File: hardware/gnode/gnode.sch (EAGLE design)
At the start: 8 parts, among them U1 ATMEGA328P_TQFP, U2 3.3V/150mA

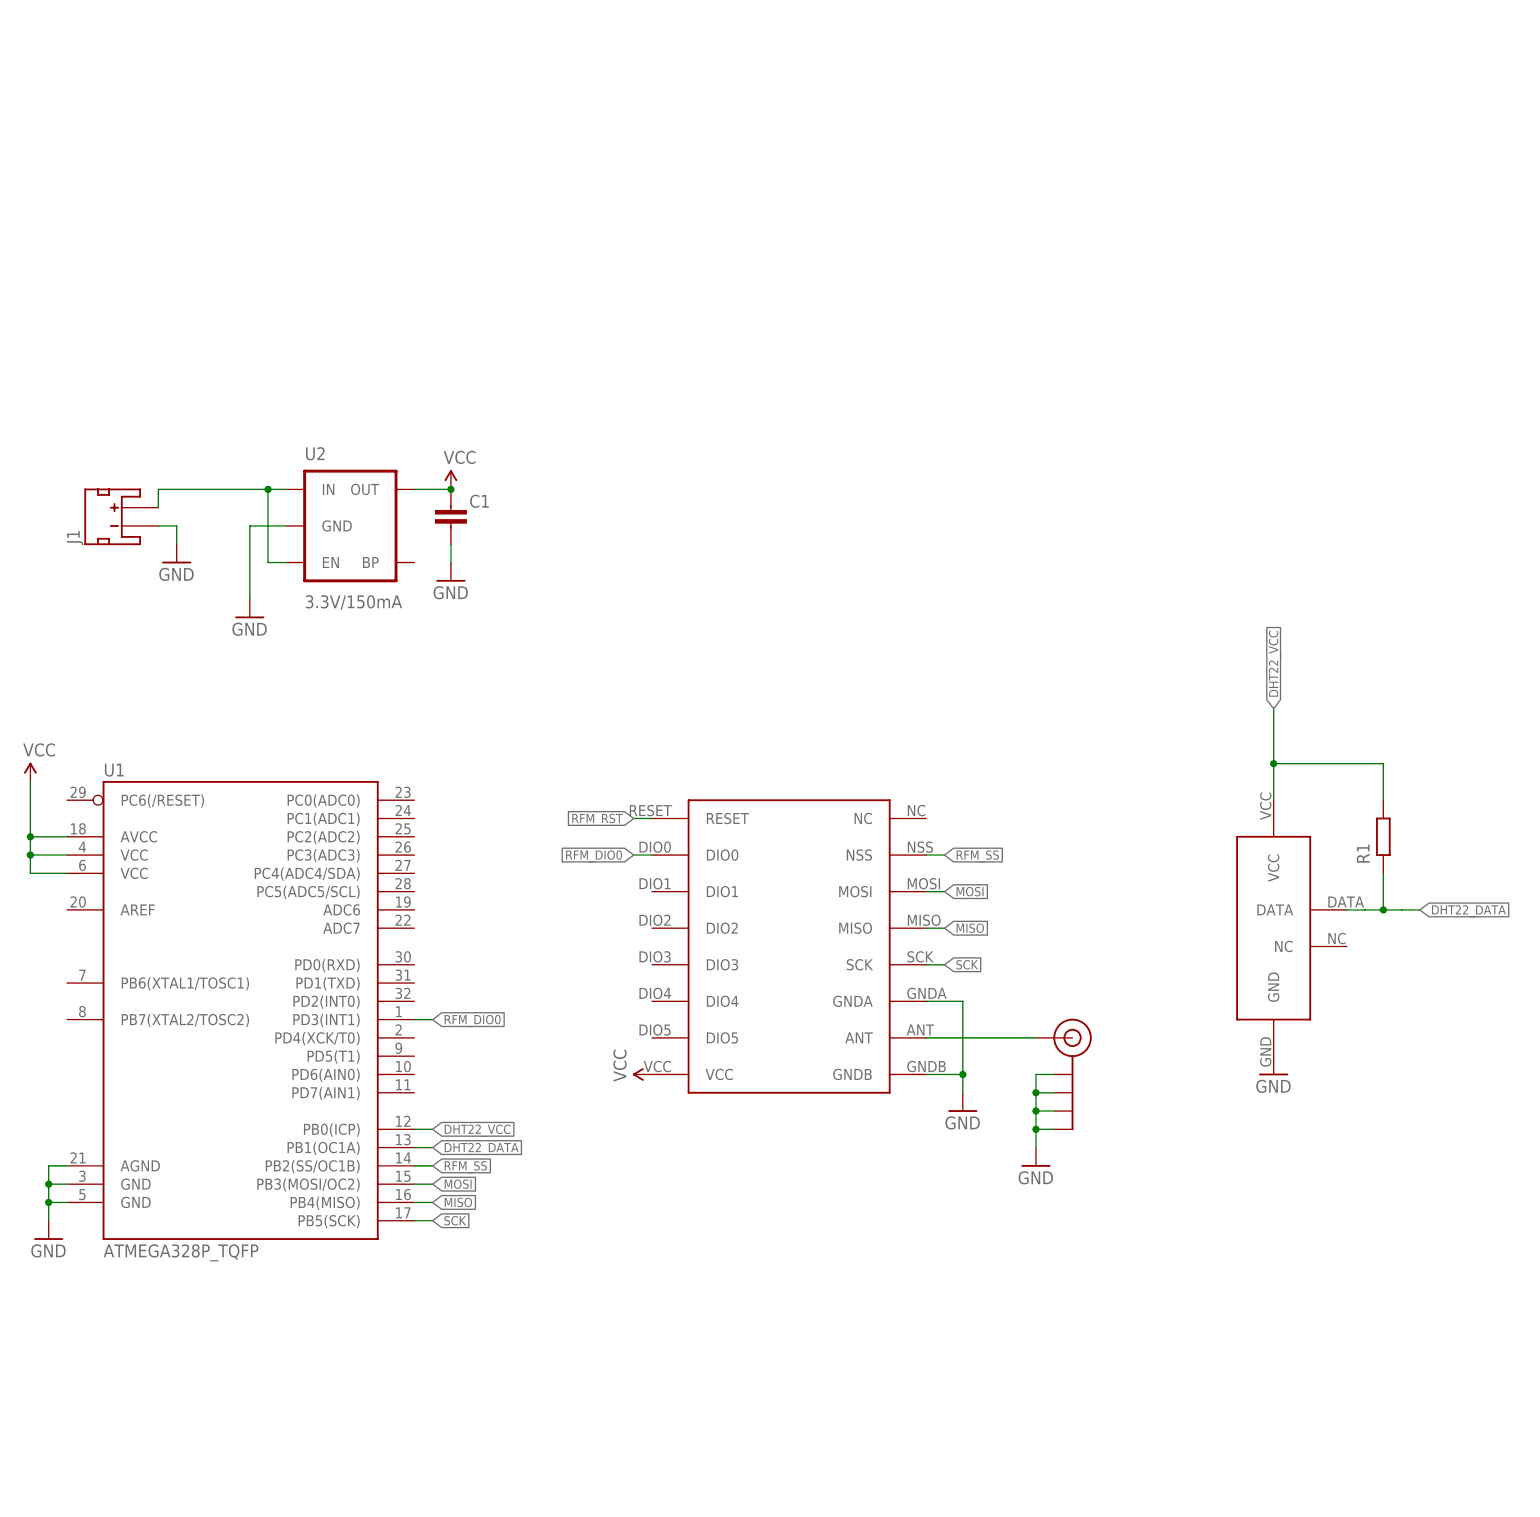
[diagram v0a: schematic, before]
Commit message: reduced to r25mm, added htu21d and icsp header
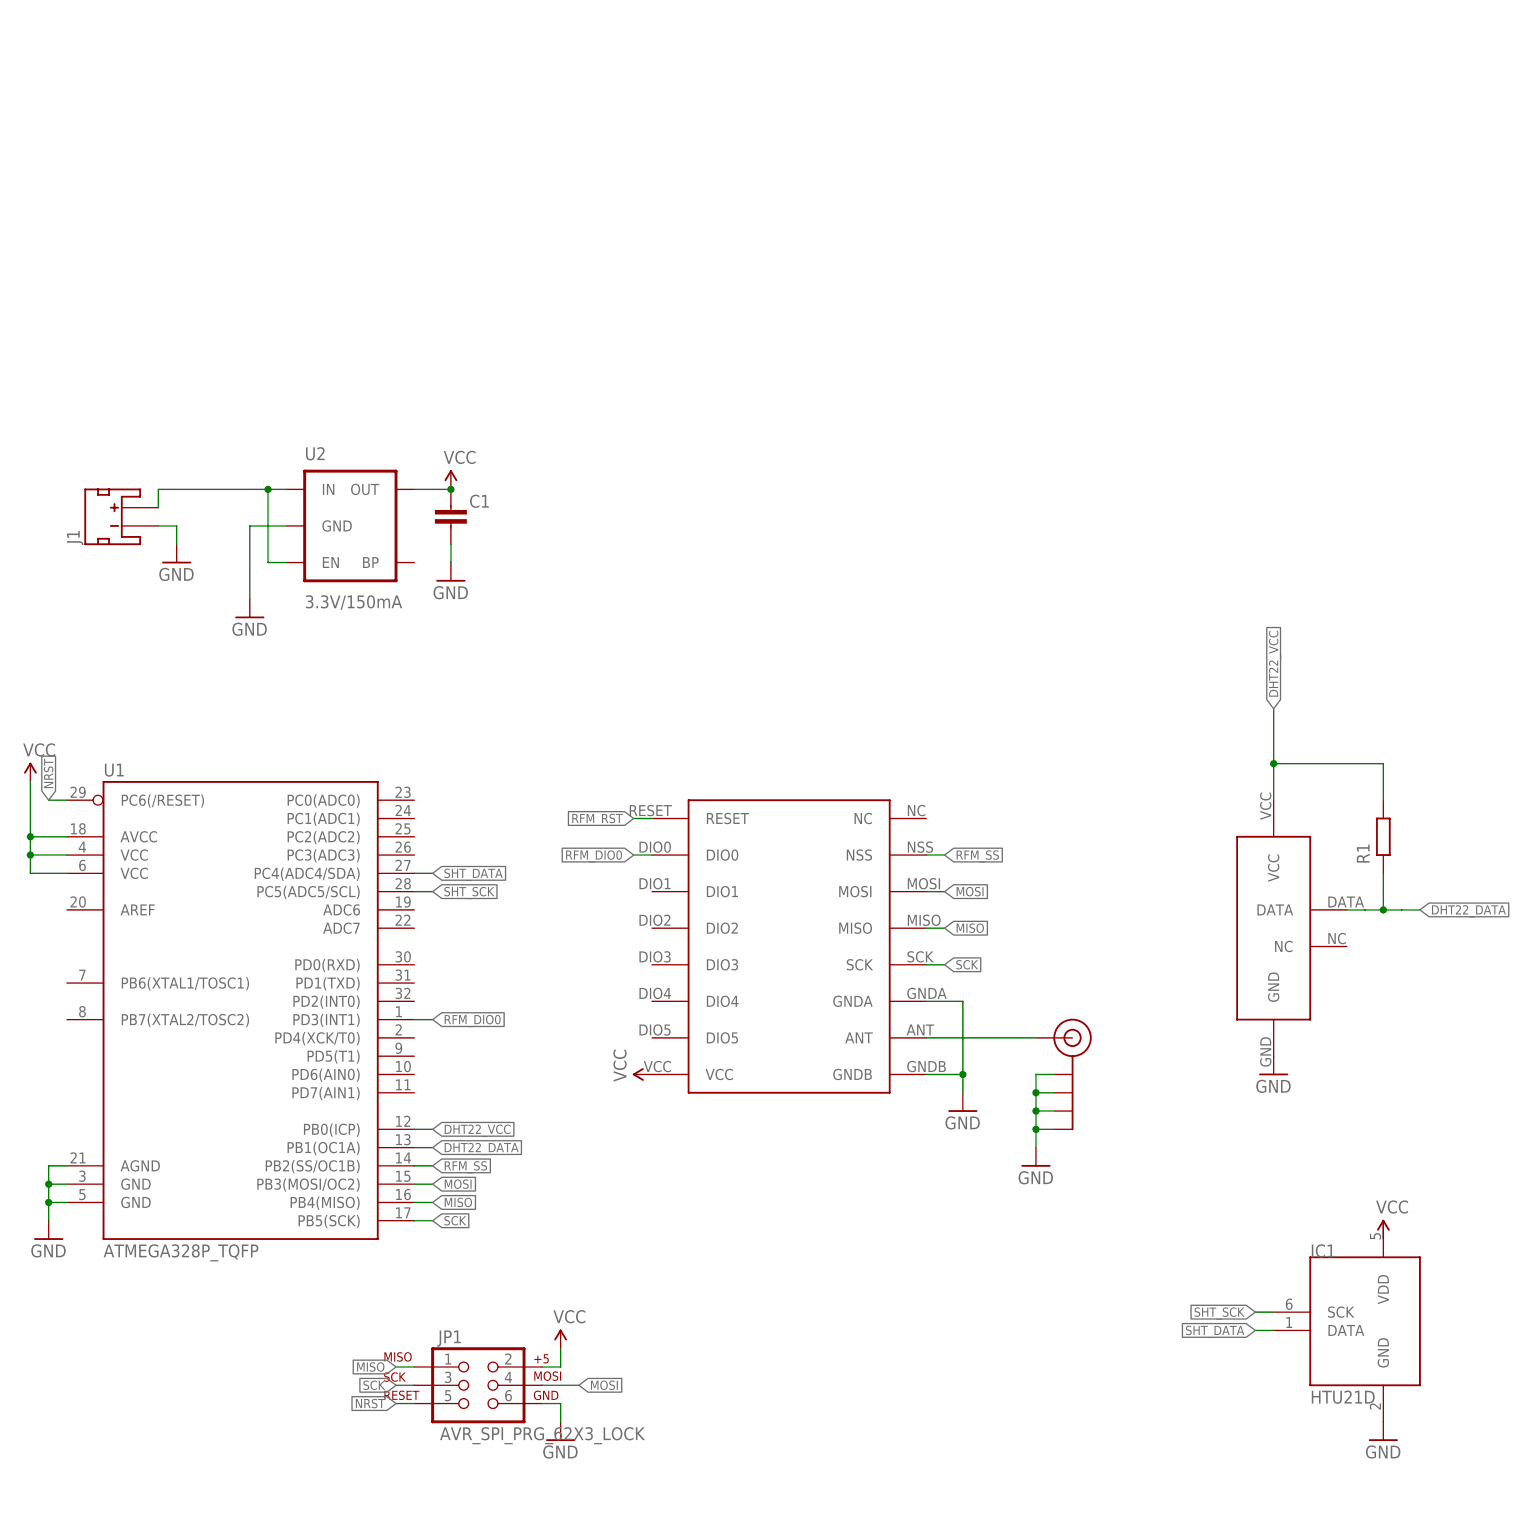
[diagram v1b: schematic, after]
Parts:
- added IC1: HTU21D, Mine:HTU21D
- added JP1: AVR_SPI_PRG_62X3_LOCK, SparkFun-Connectors:AVR_SPI_PRG_62X3_LOCK
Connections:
- new net NRST: JP1.5, U1.PC6(/RESET)
- new net SHT_DATA: IC1.DATA, U1.PC4(ADC4/SDA)
- new net SHT_SCK: IC1.SCK, U1.PC5(ADC5/SCL)
- net GND: now also IC1.GND, JP1.6
- net MISO: now also JP1.1
- net MOSI: now also JP1.4
- net SCK: now also JP1.3
- net VCC: now also JP1.2
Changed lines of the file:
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@@
 <setting verticaltext="up"/>
 </settings>
-<grid distance="0.1" unitdist="inch" unit="inch" style="lines" multiple="1" display="yes" altdistance="0.005" altunitdist="inch" altunit="inch"/>
+<grid distance="0.1" unitdist="inch" unit="inch" style="lines" multiple="1" display="no" altdistance="0.01" altunitdist="inch" altunit="inch"/>
 <layers>
 <layer number="1" name="Top" color="4" fill="1" visible="no" active="no"/>
@@
 <part name="SUPPLY3" library="SparkFun-Aesthetics" deviceset="VCC" device=""/>
 <part name="GND7" library="SparkFun-Aesthetics" deviceset="GND" device=""/>
+<part name="IC1" library="Mine" deviceset="HTU21D" device=""/>
+<part name="SUPPLY4" library="SparkFun-Aesthetics" deviceset="VCC" device=""/>
+<part name="GND8" library="SparkFun-Aesthetics" deviceset="GND" device=""/>
+<part name="JP1" library="SparkFun-Connectors" deviceset="AVR_SPI_PRG_6" device="2X3_LOCK"/>
+<part name="SUPPLY5" library="SparkFun-Aesthetics" deviceset="VCC" device=""/>
+<part name="GND9" library="SparkFun-Aesthetics" deviceset="GND" device=""/>
 </parts>
 <sheets>
@@
 <instance part="SUPPLY3" gate="G$1" x="17.78" y="109.22"/>
 <instance part="GND7" gate="1" x="17.78" y="96.52"/>
+<instance part="IC1" gate="G$1" x="142.24" y="-7.62"/>
+<instance part="SUPPLY4" gate="G$1" x="147.32" y="5.08"/>
+<instance part="GND8" gate="1" x="147.32" y="-22.86"/>
+<instance part="JP1" gate="G$1" x="20.32" y="-15.24"/>
+<instance part="SUPPLY5" gate="G$1" x="33.02" y="-10.16"/>
+<instance part="GND9" gate="1" x="33.02" y="-22.86"/>
 </instances>
 <busses>
@@
 <wire x1="17.78" y1="99.06" x2="17.78" y2="101.6" width="0.1524" layer="91"/>
 </segment>
+<segment>
+<pinref part="IC1" gate="G$1" pin="GND"/>
+<pinref part="GND8" gate="1" pin="GND"/>
+</segment>
+<segment>
+<pinref part="JP1" gate="G$1" pin="6"/>
+<pinref part="GND9" gate="1" pin="GND"/>
+<wire x1="30.48" y1="-17.78" x2="33.02" y2="-17.78" width="0.1524" layer="91"/>
+<wire x1="33.02" y1="-17.78" x2="33.02" y2="-20.32" width="0.1524" layer="91"/>
+</segment>
 </net>
 <net name="N$1" class="0">
@@
 <label x="15.24" y="12.7" size="1.27" layer="95" font="vector" xref="yes"/>
 </segment>
+<segment>
+<pinref part="JP1" gate="G$1" pin="4"/>
+<wire x1="30.48" y1="-15.24" x2="35.56" y2="-15.24" width="0.1524" layer="91"/>
+<label x="35.56" y="-15.24" size="1.27" layer="95" xref="yes"/>
+</segment>
 </net>
 <net name="MISO" class="0">
@@
 <label x="15.24" y="10.16" size="1.27" layer="95" font="vector" xref="yes"/>
 </segment>
+<segment>
+<pinref part="JP1" gate="G$1" pin="1"/>
+<wire x1="12.7" y1="-12.7" x2="10.16" y2="-12.7" width="0.1524" layer="91"/>
+<label x="10.16" y="-12.7" size="1.27" layer="95" rot="R180" xref="yes"/>
+</segment>
 </net>
 <net name="SCK" class="0">
@@
 <wire x1="12.7" y1="7.62" x2="15.24" y2="7.62" width="0.1524" layer="91"/>
 <label x="15.24" y="7.62" size="1.27" layer="95" font="vector" xref="yes"/>
+</segment>
+<segment>
+<pinref part="JP1" gate="G$1" pin="3"/>
+<wire x1="12.7" y1="-15.24" x2="10.16" y2="-15.24" width="0.1524" layer="91"/>
+<label x="10.16" y="-15.24" size="1.27" layer="95" rot="R180" xref="yes"/>
 </segment>
 </net>
@@
 <junction x="17.78" y="109.22"/>
 </segment>
+<segment>
+<pinref part="JP1" gate="G$1" pin="2"/>
+<pinref part="SUPPLY5" gate="G$1" pin="VCC"/>
+<wire x1="30.48" y1="-12.7" x2="33.02" y2="-12.7" width="0.1524" layer="91"/>
+<wire x1="33.02" y1="-12.7" x2="33.02" y2="-10.16" width="0.1524" layer="91"/>
+</segment>
 </net>
 <net name="N$2" class="0">
@@
 </segment>
 </net>
+<net name="SHT_SCK" class="0">
+<segment>
+<pinref part="IC1" gate="G$1" pin="SCK"/>
+<wire x1="132.08" y1="-5.08" x2="129.54" y2="-5.08" width="0.1524" layer="91"/>
+<label x="129.54" y="-5.08" size="1.27" layer="95" rot="R180" xref="yes"/>
+</segment>
+<segment>
+<pinref part="U1" gate="U$1" pin="PC5(ADC5/SCL)"/>
+<wire x1="12.7" y1="53.34" x2="15.24" y2="53.34" width="0.1524" layer="91"/>
+<label x="15.24" y="53.34" size="1.27" layer="95" xref="yes"/>
+</segment>
+</net>
+<net name="SHT_DATA" class="0">
+<segment>
+<pinref part="IC1" gate="G$1" pin="DATA"/>
+<wire x1="132.08" y1="-7.62" x2="129.54" y2="-7.62" width="0.1524" layer="91"/>
+<label x="129.54" y="-7.62" size="1.27" layer="95" rot="R180" xref="yes"/>
+</segment>
+<segment>
+<pinref part="U1" gate="U$1" pin="PC4(ADC4/SDA)"/>
+<wire x1="12.7" y1="55.88" x2="15.24" y2="55.88" width="0.1524" layer="91"/>
+<label x="15.24" y="55.88" size="1.27" layer="95" xref="yes"/>
+</segment>
+</net>
+<net name="NRST" class="0">
+<segment>
+<pinref part="JP1" gate="G$1" pin="5"/>
+<wire x1="12.7" y1="-17.78" x2="10.16" y2="-17.78" width="0.1524" layer="91"/>
+<label x="10.16" y="-17.78" size="1.27" layer="95" rot="R180" xref="yes"/>
+</segment>
+<segment>
+<pinref part="U1" gate="U$1" pin="PC6(/RESET)"/>
+<wire x1="-35.56" y1="66.04" x2="-38.1" y2="66.04" width="0.1524" layer="91"/>
+<label x="-38.1" y="66.04" size="1.27" layer="95" rot="R90" xref="yes"/>
+</segment>
+</net>

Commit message: switched to mcp1700
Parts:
- removed U2: 3.3V/150mA, SparkFun-PowerIC:V_REG_MIC52053.3V
- added C2: 1u, passives-7351:CAPACITOR0603-N
- added U$3: MCP1700TT, dtb:MCP1700TT
- C1: value (none) -> 1u
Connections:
- net GND: now also C2.2, U$3.GND; no longer U2.GND
- net N$2: now also C2.1, U$3.IN; no longer U2.EN, U2.IN
- net VCC: now also U$3.OUT; no longer U2.OUT
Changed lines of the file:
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@@
 <part name="J1" library="dtb" deviceset="JST_2MM_MALE_TH" device=""/>
 <part name="GND5" library="SparkFun-Aesthetics" deviceset="GND" device=""/>
-<part name="U2" library="SparkFun-PowerIC" deviceset="V_REG_MIC5205" device="3.3V" value="3.3V/150mA"/>
 <part name="GND6" library="SparkFun-Aesthetics" deviceset="GND" device=""/>
-<part name="C1" library="passives-7351" deviceset="CAPACITOR" device="0603-N"/>
+<part name="C1" library="passives-7351" deviceset="CAPACITOR" device="0603-N" value="1u"/>
 <part name="SUPPLY3" library="SparkFun-Aesthetics" deviceset="VCC" device=""/>
 <part name="GND7" library="SparkFun-Aesthetics" deviceset="GND" device=""/>
@@
 <part name="SUPPLY5" library="SparkFun-Aesthetics" deviceset="VCC" device=""/>
 <part name="GND9" library="SparkFun-Aesthetics" deviceset="GND" device=""/>
+<part name="U$3" library="dtb" deviceset="MCP1700" device="TT"/>
+<part name="C2" library="passives-7351" deviceset="CAPACITOR" device="0603-N" value="1u"/>
 </parts>
 <sheets>
@@
 <instance part="GND4" gate="1" x="-38.1" y="5.08"/>
 <instance part="J1" gate="G$1" x="-27.94" y="104.14" rot="R90"/>
-<instance part="GND5" gate="1" x="-20.32" y="99.06"/>
-<instance part="U2" gate="U1" x="5.08" y="104.14"/>
-<instance part="GND6" gate="1" x="-10.16" y="91.44"/>
+<instance part="GND5" gate="1" x="-20.32" y="93.98"/>
+<instance part="GND6" gate="1" x="-2.54" y="93.98"/>
 <instance part="C1" gate="G$1" x="17.78" y="106.68"/>
 <instance part="SUPPLY3" gate="G$1" x="17.78" y="109.22"/>
-<instance part="GND7" gate="1" x="17.78" y="96.52"/>
+<instance part="GND7" gate="1" x="17.78" y="93.98"/>
 <instance part="IC1" gate="G$1" x="142.24" y="-7.62"/>
 <instance part="SUPPLY4" gate="G$1" x="147.32" y="5.08"/>
@@
 <instance part="SUPPLY5" gate="G$1" x="33.02" y="-10.16"/>
 <instance part="GND9" gate="1" x="33.02" y="-22.86"/>
+<instance part="U$3" gate="G$1" x="-2.54" y="109.22"/>
+<instance part="C2" gate="G$1" x="-15.24" y="106.68"/>
 </instances>
 <busses>
@@
 <pinref part="GND5" gate="1" pin="GND"/>
 <wire x1="-22.86" y1="104.14" x2="-20.32" y2="104.14" width="0.1524" layer="91"/>
-<wire x1="-20.32" y1="104.14" x2="-20.32" y2="101.6" width="0.1524" layer="91"/>
-</segment>
-<segment>
-<pinref part="U2" gate="U1" pin="GND"/>
-<pinref part="GND6" gate="1" pin="GND"/>
-<wire x1="-5.08" y1="104.14" x2="-10.16" y2="104.14" width="0.1524" layer="91"/>
-<wire x1="-10.16" y1="104.14" x2="-10.16" y2="93.98" width="0.1524" layer="91"/>
+<wire x1="-20.32" y1="104.14" x2="-20.32" y2="96.52" width="0.1524" layer="91"/>
 </segment>
 <segment>
 <pinref part="C1" gate="G$1" pin="2"/>
 <pinref part="GND7" gate="1" pin="GND"/>
-<wire x1="17.78" y1="99.06" x2="17.78" y2="101.6" width="0.1524" layer="91"/>
+<wire x1="17.78" y1="96.52" x2="17.78" y2="101.6" width="0.1524" layer="91"/>
 </segment>
 <segment>
@@
 <wire x1="30.48" y1="-17.78" x2="33.02" y2="-17.78" width="0.1524" layer="91"/>
 <wire x1="33.02" y1="-17.78" x2="33.02" y2="-20.32" width="0.1524" layer="91"/>
+</segment>
+<segment>
+<pinref part="U$3" gate="G$1" pin="GND"/>
+<pinref part="GND6" gate="1" pin="GND"/>
+<wire x1="-2.54" y1="101.6" x2="-2.54" y2="99.06" width="0.1524" layer="91"/>
+<pinref part="C2" gate="G$1" pin="2"/>
+<wire x1="-2.54" y1="99.06" x2="-2.54" y2="96.52" width="0.1524" layer="91"/>
+<wire x1="-15.24" y1="101.6" x2="-15.24" y2="99.06" width="0.1524" layer="91"/>
+<wire x1="-15.24" y1="99.06" x2="-2.54" y2="99.06" width="0.1524" layer="91"/>
+<junction x="-2.54" y="99.06"/>
 </segment>
 </net>
@@
 </segment>
 <segment>
-<pinref part="U2" gate="U1" pin="OUT"/>
 <pinref part="C1" gate="G$1" pin="1"/>
-<wire x1="12.7" y1="109.22" x2="17.78" y2="109.22" width="0.1524" layer="91"/>
+<wire x1="5.08" y1="109.22" x2="17.78" y2="109.22" width="0.1524" layer="91"/>
 <pinref part="SUPPLY3" gate="G$1" pin="VCC"/>
 <junction x="17.78" y="109.22"/>
+<pinref part="U$3" gate="G$1" pin="OUT"/>
 </segment>
 <segment>
@@
 <net name="N$2" class="0">
 <segment>
-<pinref part="U2" gate="U1" pin="IN"/>
 <pinref part="J1" gate="G$1" pin="+"/>
-<wire x1="-5.08" y1="109.22" x2="-7.62" y2="109.22" width="0.1524" layer="91"/>
-<wire x1="-7.62" y1="109.22" x2="-22.86" y2="109.22" width="0.1524" layer="91"/>
+<wire x1="-10.16" y1="109.22" x2="-7.62" y2="109.22" width="0.1524" layer="91"/>
+<wire x1="-7.62" y1="109.22" x2="-15.24" y2="109.22" width="0.1524" layer="91"/>
+<wire x1="-15.24" y1="109.22" x2="-22.86" y2="109.22" width="0.1524" layer="91"/>
 <wire x1="-22.86" y1="109.22" x2="-22.86" y2="106.68" width="0.1524" layer="91"/>
-<pinref part="U2" gate="U1" pin="EN"/>
-<wire x1="-5.08" y1="99.06" x2="-7.62" y2="99.06" width="0.1524" layer="91"/>
-<wire x1="-7.62" y1="99.06" x2="-7.62" y2="109.22" width="0.1524" layer="91"/>
-<junction x="-7.62" y="109.22"/>
-</segment>
-</net>
+<pinref part="U$3" gate="G$1" pin="IN"/>
+<pinref part="C2" gate="G$1" pin="1"/>
+<junction x="-15.24" y="109.22"/>
+</segment>
+</net>
